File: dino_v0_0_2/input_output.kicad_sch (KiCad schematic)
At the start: 27 parts, among them SW1 SW_DIP_x08

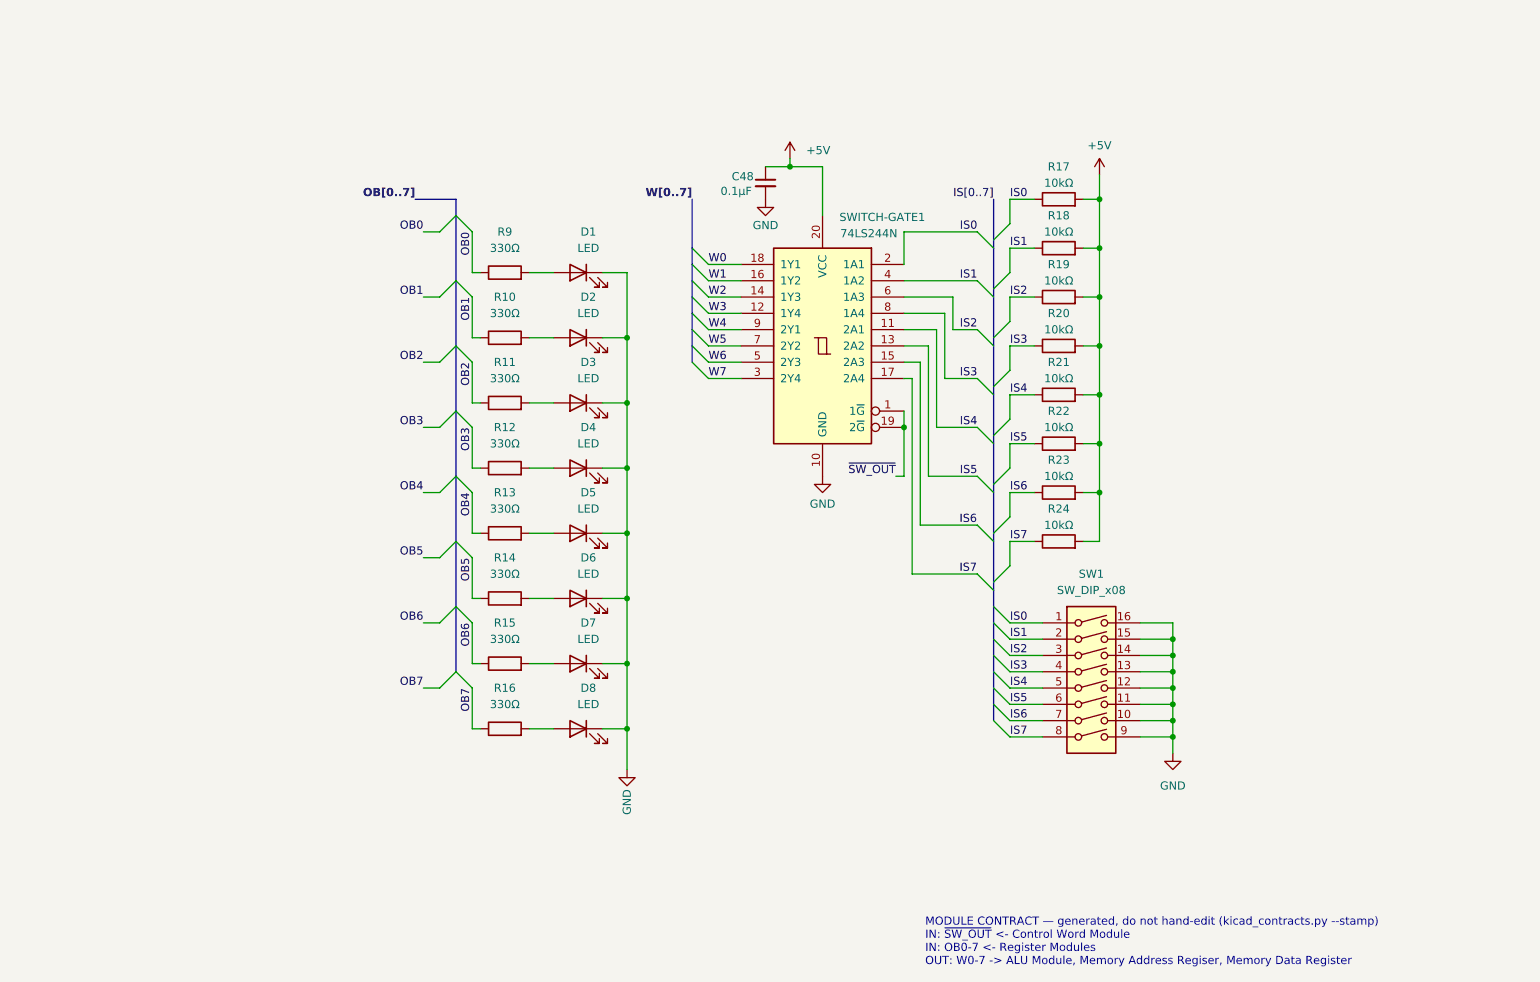
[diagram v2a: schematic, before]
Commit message: feat: phase E step A -- the 16K I/O window, in schematic
Carves 0x4000-0x7FFF out of ROM space and publishes a bus. The ROM now
answers 0x0000-0x3FFF only; the window decodes to no core chip, so W
reads its park -- 0xFF, which is HALT.

TWO NEW PACKAGES, both on the memory board:

  U74 '00  ~{M14}      = NAND(M14, M14)
           ~{ROM_SEL}  = NAND(~{RAM_EN}, ~{M14})
           ~{RAM_OE_G} = NAND(RAM_OE_ON, M15)
           ~{IO_SEL}   = NAND(~{RAM_EN}, M14)
  U75 '32  ~{IO_RD}    = OR(~{IO_SEL}, READS_IDLE)
           ~{IO_WR}    = OR(~{IO_SEL}, ~{RAM_WRITE_EN})
           RESET_B     = OR(RESET, GND)
           ~{IO_RD_Q}  = OR(~{IO_RD}, CLK)

Eight copper changes: U24.20 and U22.12 to ~{ROM_SEL}, U26.22/U51.9 fed
from U74 g3, U39.10 to ~{IO_RD}, U37.10 and U28.7 unlanded, U37.11 to
GND. Park: R4-R8 + R25-R27, 4.7k on W0-7. CLK crosses through R3, 100R,
source end -- the R2 treatment.

IN RETIRES. ~{SW_OUT} has zero pins project-wide. SWITCH-GATE1's enables
are strapped +5V until card zero drives them from an address decode.

THE ROM_EN ALIAS IS DELETED. Once U24.20 moved, ROM_EN named a net with
no ROM consumer. Deleting it half-way SPLIT the net and alias_splits()
caught it mid-edit -- M15: ['M15', 'M15/ROM_EN'], the exact two-key
failure that once cost this project the ROM chip-enable on every
continuity checklist ever generated.

CLK WAS A FOURTH CROSSING THE SPEC DID NOT CARRY. Census: 15 CLK pins,
none on the memory board; ~{CLK} at U51.4 is the wrong polarity and both
new packages are full. SECTION 1's cost table predated the read-term
split that spent U75 g4, so memory is +4 and MDR is +4 -- the wire margin
is zero. Ruled: stay on memory, the output-load argument still holds.

SWITCH-GATE1/SW1/R17-R24/C48 move to their own input.kicad_sch so the
DIP card is modelled as a card. No renumbering: 168 designators
unchanged, --since reports annotate=0.

TOOLING RECONCILED TO THE DESIGN, not the reverse:
  test_continuity_completeness  M15_PINS U24.20 -> U74.10; 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
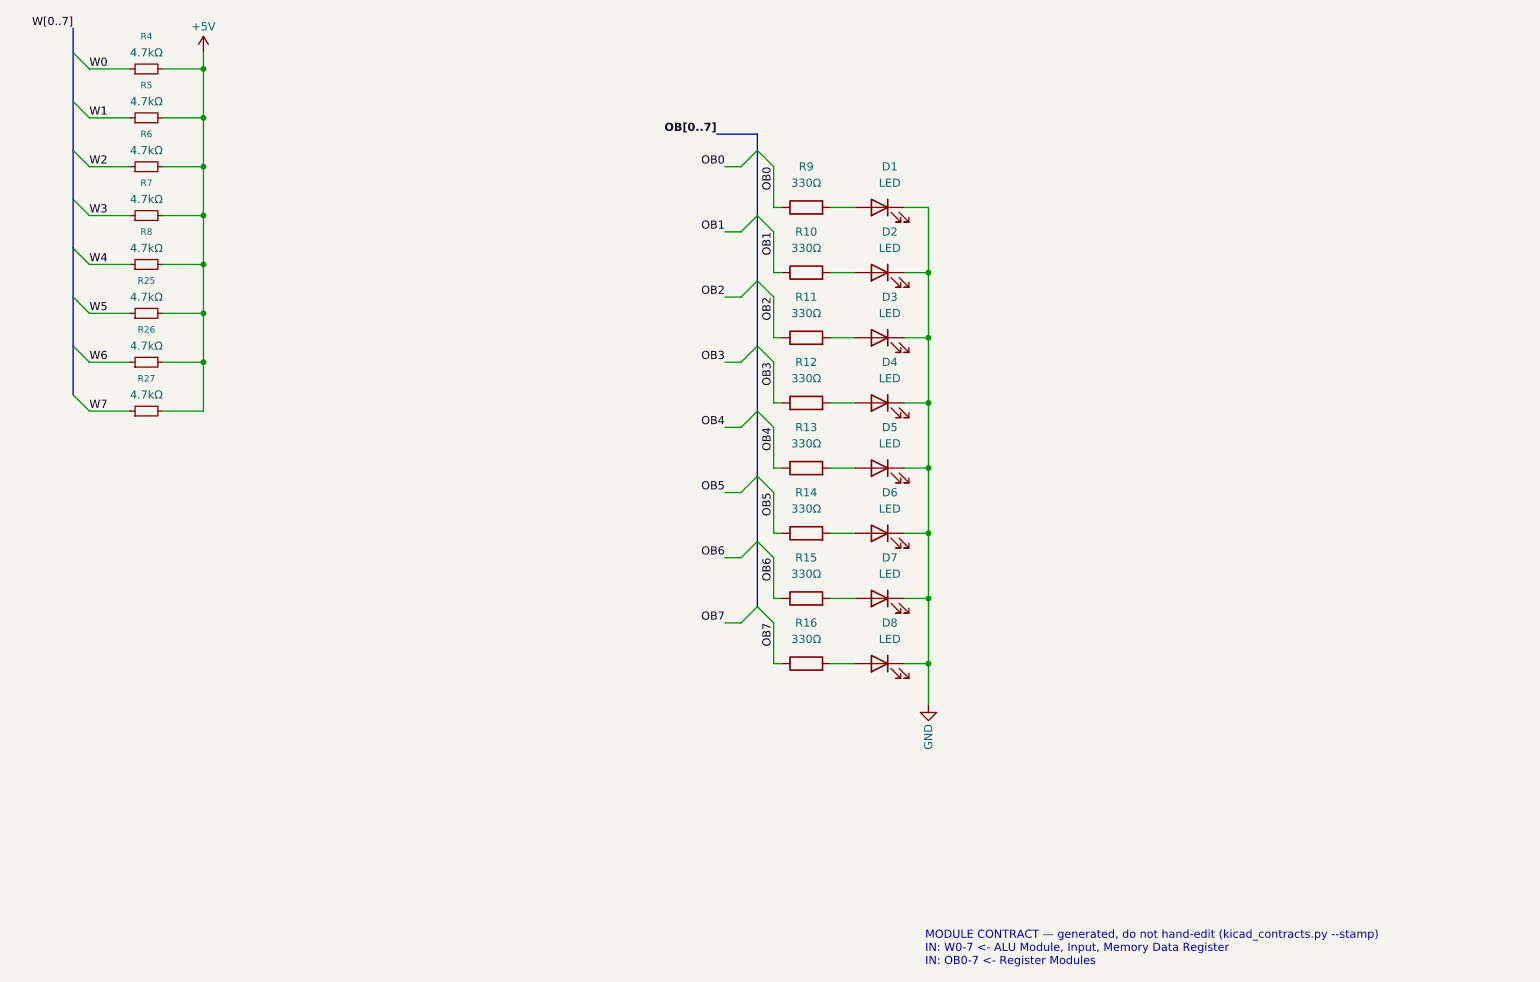
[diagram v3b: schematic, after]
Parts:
- removed C48: 0.1µF, symbol Device:C_Small
- removed R17, R18, R19, R20, R21, R22, R23, R24: 10kΩ, symbol Device:R
- removed SW1: SW_DIP_x08, symbol Switch:SW_DIP_x08
- removed SWITCH-GATE1: 74LS244N, symbol 74xx:74LS244N
- added R25, R26, R27, R4, R5, R6, R7, R8: 4.7kΩ, symbol Device:R_Small
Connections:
- net +5V: now also R25.2, R26.2, R27.2, R4.2, R5.2, R6.2, R7.2, R8.2
- net W0: now also R4.1
- net W1: now also R5.1
- net W2: now also R6.1
- net W3: now also R7.1
- net W4: now also R8.1
- net W5: now also R25.1
- net W6: now also R26.1
- net W7: now also R27.1
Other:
- note added: "MODULE CONTRACT — generated, do not hand-edit (kicad_contracts.py --stamp) IN: W0-7 <- ALU Module, Input, Memory Data Register IN: OB0-7 <- Register Modules"
- note removed: "MODULE CONTRACT — generated, do not hand-edit (kicad_contracts.py --stamp) IN: ~{SW_OUT} <- Control Word Module IN: OB0-7 <- Register Modules OUT: W0-7 -> ALU Module, Memory Address Regiser, Memory Data Register"
- moved on the sheet: D1, D2, D3, D4, D5, D6, D7, D8, R10, R11, R12, R13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
